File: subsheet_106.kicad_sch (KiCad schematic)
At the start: 0 parts

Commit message: information schéma, commence le gate array I29
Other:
- title: (none) -> Conversion du Thomson MO5 — Unité centrale
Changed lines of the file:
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@@
   (paper "A4" portrait)
   (title_block
+    (title "Conversion du Thomson MO5 — Unité centrale")
     (date "2023-05-12")
     (rev "DRAFT")
+    (comment 1 "http://github.com/sporniket/kicad-conversions--thomson-mo5--v1")
+    (comment 2 "Dépôt d'origine : ")
+    (comment 4 "Reference : POP5001 501994-01")
   )
   (symbol (lib_id "power:PWR_FLAG") (at 177.8 25.4 180) (unit 1)

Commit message: remise au propre
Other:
- title: Conversion du Thomson MO5 — Unité centrale -> Conversion du Thomson MO5 — Unité centrale v1
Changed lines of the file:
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@@
   (paper "A4" portrait)
   (title_block
-    (title "Conversion du Thomson MO5 — Unité centrale")
-    (date "2023-05-12")
+    (title "Conversion du Thomson MO5 — Unité centrale v1")
+    (date "2023-05-14")
     (rev "DRAFT")
     (comment 1 "http://github.com/sporniket/kicad-conversions--thomson-mo5--v1")
-    (comment 2 "Dépôt d'origine : ")
+    (comment 3 "Gate Array Motorola MCA 1300 ALS")
     (comment 4 "Reference : POP5001 501994-01")
   )

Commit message: début des horloges
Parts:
- added C38, C51, C? (x4): 47nF, symbol Device:C_Small
- added C?: 10nF, symbol Device:C_Small
- added C?: 100uF, symbol Device:C_Polarized_Small
- added D?: 1N4148, symbol Device:D_Small
- added I45: 74LS74 Double Flip-Flop 'D', Package_DIP:DIP-14_W7.62mm_LongPads, symbol 74x74:74LS74_DUAL_POSITIVE-EDGE-TRIGGERED_D_FLIP-FLOPS_WITH_PRESET_CLEAR_AND_CO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
- added I46: 74LS157 4×2:1 Multiplexeur, Package_DIP:DIP-16_W7.62mm_LongPads, symbol 74x157:QUADRUPLE_2-LINE_TO_1-LINE_DATA_SELECTORS_MULTIPLEXERS_PHY
- added I47: 74LS211 Double multi-vibrateur monostable, Package_DIP:DIP-16_W7.62mm_LongPads, symbol 74x221:DUAL_MONOSTABLE_MULTIVIBRATORS_WITH_SCHMITT-TRIGGER_INPUTS_PHY
- added R?: 3K3, symbol Device:R_Small
- added R?: 1K, symbol Device:R_Small
- added R?: ?10K, symbol Device:R_Small
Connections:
- new net: I45.13 (~{2CLR}), R?.1
- new net: I45.9 (2Q), I46.1 (~{A}/B)
- new net +5V: C38.2, C51.2, C?.1, C?.2, C?.2, I45.14 (VCC), I45.2 (1D), I45.4 (~{1PRE}), I46.10 (3B), I46.16 (VCC), I46.6 (2B), I47.16 (VCC), R?.2
- new net ??AAA: I45.5 (1Q)
- new net E: I45.11 (2CLK)
- new net E/CLRG: I46.5 (2A)
- new net GND: C38.1, C51.1, C?.1, C?.1, C?.2, I45.7 (GND), I46.14 (4A), I46.8 (GND), I47.8 (GND)
- new net H16: I46.4 (1Y)
- new net H/VCO-16MHz: I46.2 (1A)
- new net J/~{RESET}: I45.10 (~{2PRE})
- new net Q: I45.3 (1CLK)
- new net ~{SYCL}: I45.1 (~{1CLR}), I46.7 (2Y)
- no-connect marks 0 -> 2
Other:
- note added: "De I48-CB2"
- note added: "Mettre I21 + Q01 (16MHz)"
- note added: "Vers I12"
- note added: "Vers I12-11 Vers I16-9"

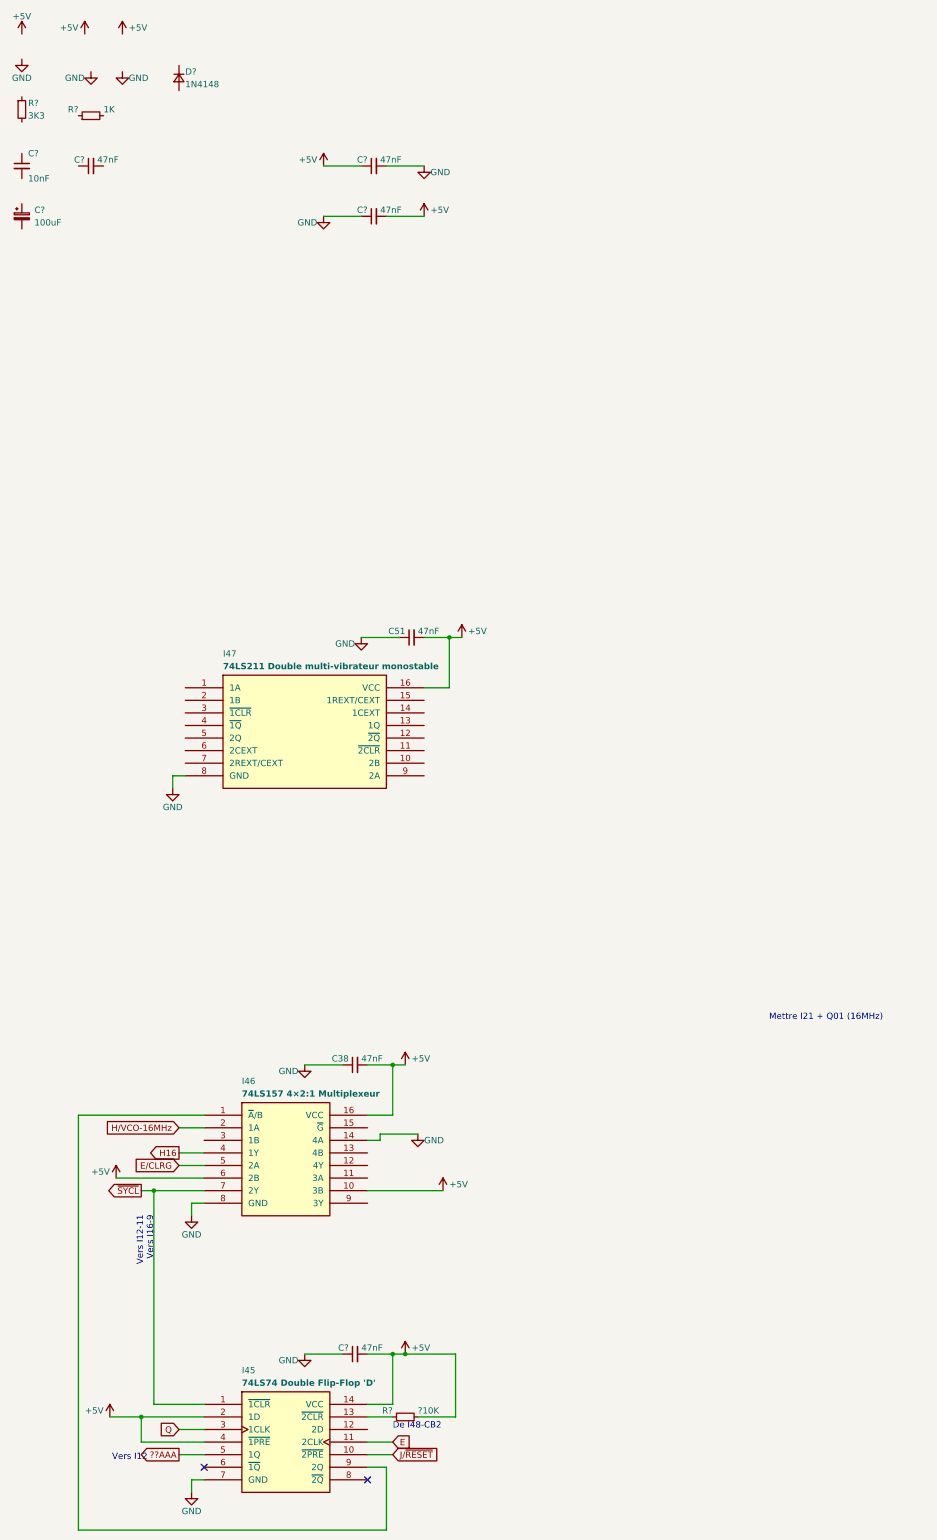
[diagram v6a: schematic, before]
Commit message: continue l'horlogerie : 16 MHz
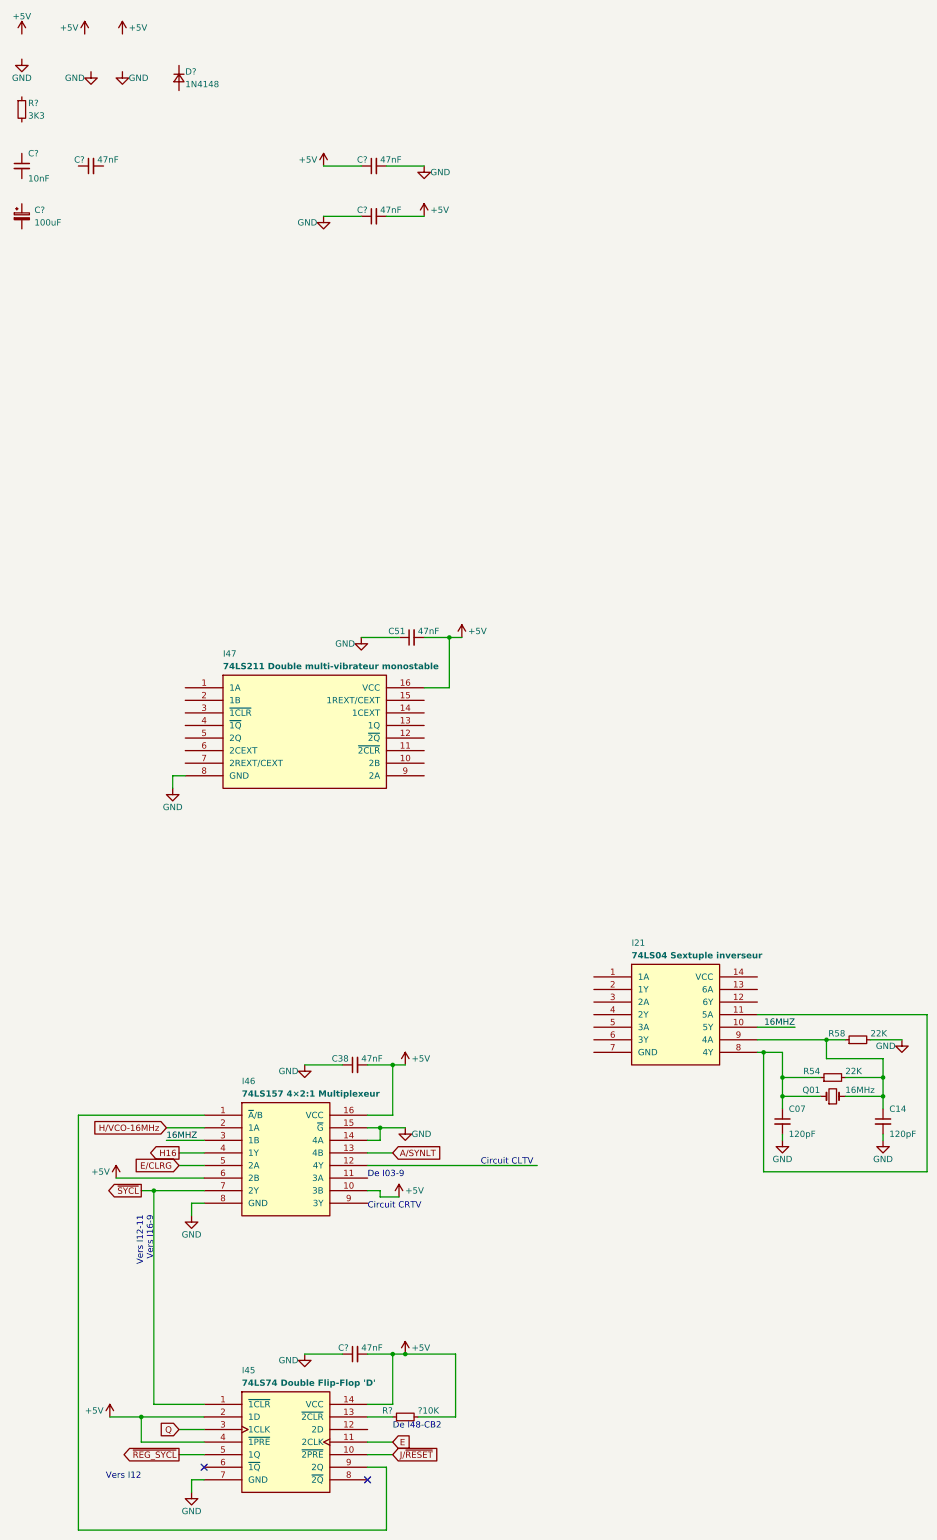
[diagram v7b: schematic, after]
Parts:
- added C07, C14: 120pF, symbol Device:C_Small
- added I21: 74LS04 Sextuple inverseur, Package_DIP:DIP-14_W7.62mm_LongPads, symbol 74x04:74X04_HEX_INVERTER_PHY
- added Q01: 16MHz, symbol Device:Crystal_Small
- added R58: 22K, symbol Device:R_Small
- R54: renamed from R?; value 1K -> 22K
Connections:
- net GND: now also I46.15 (~{G}), C07.2, C14.2, R58.2
- net at R54.1: now also C07.1, I21.11 (5A), I21.8 (4Y), Q01.1
- net at R54.2: now also C14.1, I21.9 (4A), Q01.2, R58.1
- net A/SYNLT: now reaches I46.13 (4B)
- net 16MHZ: now reaches I46.3 (1B)
- net 16MHZ: now also I21.10 (5Y)
- net ??AAA renamed ~{REG_SYCL}
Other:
- note added: "Circuit CLTV"
- note added: "Circuit CRTV"
- note added: "De I03-9"
- note removed: "Mettre I21 + Q01 (16MHz)"
- moved on the sheet: R54

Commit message: horloges : generation CRTV, CLTV
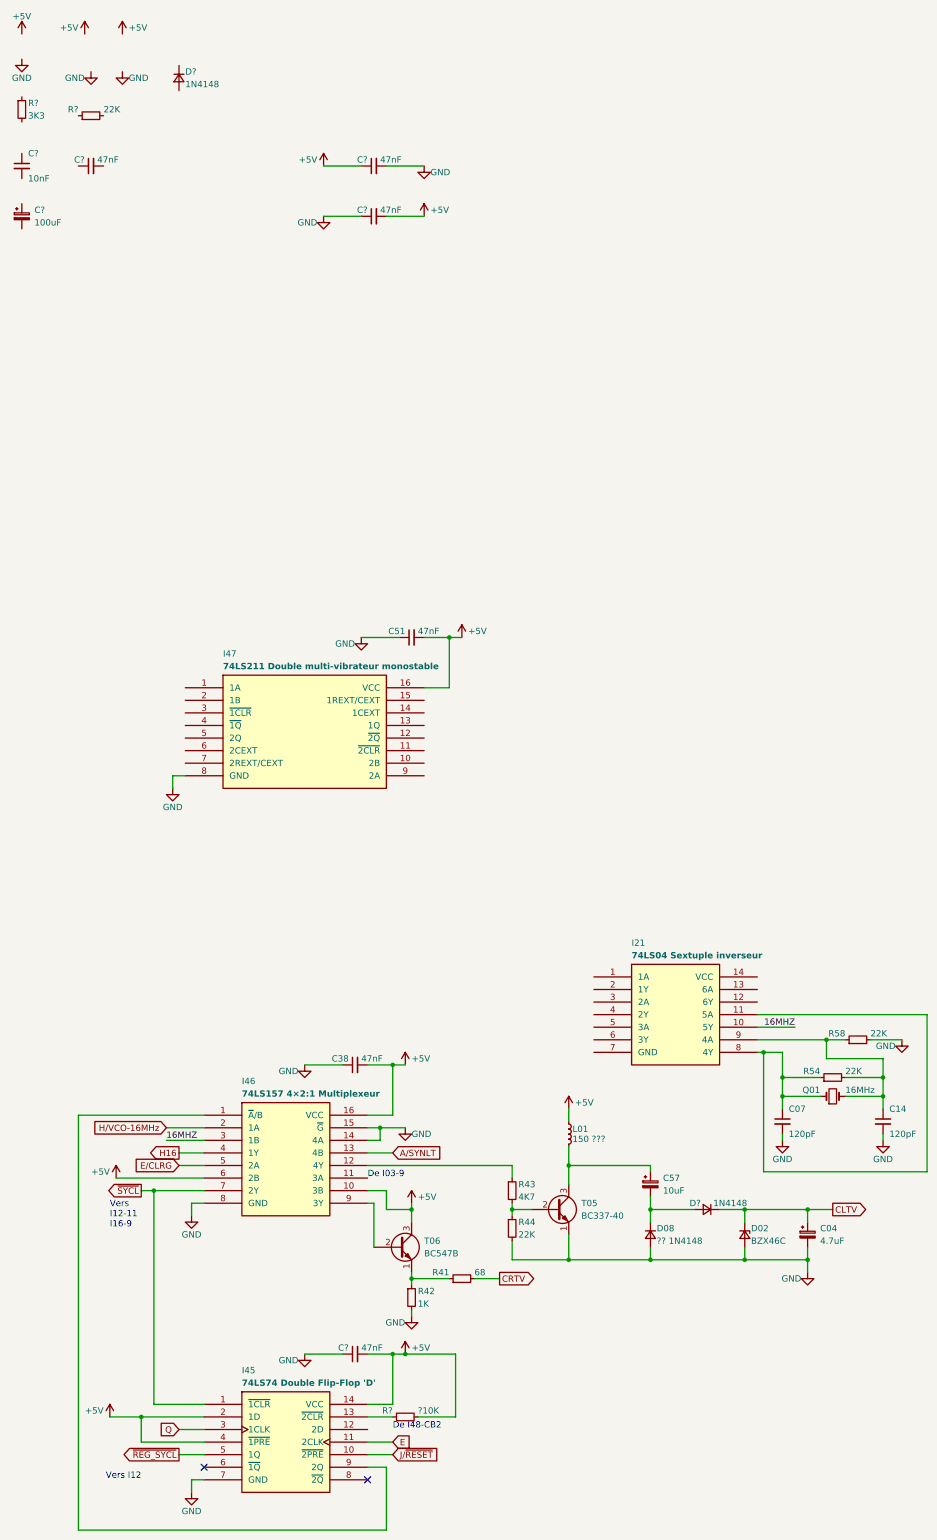
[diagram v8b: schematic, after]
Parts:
- added C04: 4.7uF, symbol Device:C_Polarized_Small
- added C57: 10uF, symbol Device:C_Polarized_Small
- added D02: BZX46C, symbol Device:D_Zener_Small
- added D08: ?? 1N4148, symbol Device:D_Small
- added D?: 1N4148, symbol Device:D_Small
- added L01: 150 ???, symbol Device:L_Small
- added R41: 68, symbol Device:R_Small
- added R42: 1K, symbol Device:R_Small
- added R43: 4K7, symbol Device:R_Small
- added R44, R?: 22K, symbol Device:R_Small
- added T05: BC337-40, symbol Device:Q_NPN_EBC
- added T06: BC547B, symbol Device:Q_NPN_EBC
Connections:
- net +5V: now also L01.1, T06.3 (C)
- net GND: now also C04.2, D02.2 (A), D08.2 (A), R42.2, R44.2, T05.1 (E)
- net at I46.12 (4Y): now also R43.1
- net at I46.9 (3Y): now also T06.2 (B)
- new net: R41.1, R42.1, T06.1 (E)
- new net: R43.2, R44.1, T05.2 (B)
- new net: C57.1, L01.2, T05.3 (C)
- new net: C57.2, D08.1 (K), D?.2 (A)
- new net CLTV: C04.1, D02.1 (K), D?.1 (K)
- new net CRTV: R41.2
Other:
- note added: "Vers I12-11 I16-9"
- note removed: "Circuit CLTV"
- note removed: "Circuit CRTV"
- note removed: "Vers I12-11 Vers I16-9"
